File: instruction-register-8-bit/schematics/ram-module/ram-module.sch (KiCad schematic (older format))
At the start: 19 parts

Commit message: updated annotations
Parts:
- gave numbers to parts that had none: 15
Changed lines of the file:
@@
 $EndDescr
 $Comp
-L common-symbols:UM61512A U?
+L common-symbols:UM61512A U4
 U 1 1 60FE2046
 P 5375 2100
-F 0 "U?" V 5400 2125 50  0000 L CNN
+F 0 "U4" V 5400 2125 50  0000 L CNN
 F 1 "UM61512A" V 5725 800 50  0000 L CNN
 F 2 "" H 5625 0   50  0001 C CNN
@@
 $EndComp
 $Comp
-L 74xx:74LS245 U?
+L 74xx:74LS245 U5
 U 1 1 60FE803A
 P 6425 4525
-F 0 "U?" V 6700 3875 50  0000 R CNN
+F 0 "U5" V 6700 3875 50  0000 R CNN
 F 1 "74LS245" V 6525 4700 50  0000 R CNN
 F 2 "" H 6425 4525 50  0001 C CNN
@@
 	4750 1475 4750 2000
 $Comp
-L 74xx:74LS257 U?
+L 74xx:74LS257 U1
 U 1 1 61003633
 P 2050 4475
-F 0 "U?" V 2325 3650 50  0000 R CNN
+F 0 "U1" V 2325 3650 50  0000 R CNN
 F 1 "74LS257" V 2050 4625 50  0000 R CNN
 F 2 "" H 2050 4475 50  0001 C CNN
@@
 $EndComp
 $Comp
-L 74xx:74LS257 U?
+L 74xx:74LS257 U2
 U 1 1 60FF65B7
 P 4125 4475
-F 0 "U?" V 4400 3650 50  0000 R CNN
+F 0 "U2" V 4400 3650 50  0000 R CNN
 F 1 "74LS257" V 4125 4625 50  0000 R CNN
 F 2 "" H 4125 4475 50  0001 C CNN
@@
 Connection ~ 6625 5450
 $Comp
-L Switch:SW_DIP_x08 SW?
+L Switch:SW_DIP_x08 SW1
 U 1 1 6103D073
 P 1025 6625
-F 0 "SW?" H 950 6175 50  0000 L CNN
+F 0 "SW1" H 950 6175 50  0000 L CNN
 F 1 "SW_DIP_x08" H 800 7200 50  0000 L CNN
 F 2 "" H 1025 6625 50  0001 C CNN
@@
 Connection ~ 625  6925
 $Comp
-L power:GND #PWR?
+L power:GND #PWR01
 U 1 1 6105BB53
 P 625 7025
-F 0 "#PWR?" H 625 6775 50  0001 C CNN
+F 0 "#PWR01" H 625 6775 50  0001 C CNN
 F 1 "GND" H 630 6852 50  0000 C CNN
 F 2 "" H 625 7025 50  0001 C CNN
@@
 	6925 5025 7150 5025
 $Comp
-L 74xx:74LS04 U?
+L 74xx:74LS04 U3
 U 1 1 610C85D1
 P 8425 4625
-F 0 "U?" H 8425 4308 50  0000 C CNN
+F 0 "U3" H 8425 4308 50  0000 C CNN
 F 1 "74LS04" H 8425 4399 50  0000 C CNN
 F 2 "" H 8425 4625 50  0001 C CNN
@@
 $EndComp
 $Comp
-L 74xx:74LS08 U?
+L 74xx:74LS08 U7
 U 1 1 610CBDAF
 P 9100 4625
-F 0 "U?" H 9100 4308 50  0000 C CNN
+F 0 "U7" H 9100 4308 50  0000 C CNN
 F 1 "74LS08" H 9100 4399 50  0000 C CNN
 F 2 "" H 9100 4625 50  0001 C CNN
@@
 RAMe
 $Comp
-L power:GND #PWR?
+L power:GND #PWR09
 U 1 1 610E4B12
 P 7225 5075
-F 0 "#PWR?" H 7225 4825 50  0001 C CNN
+F 0 "#PWR09" H 7225 4825 50  0001 C CNN
 F 1 "GND" H 7230 4902 50  0000 C CNN
 F 2 "" H 7225 5075 50  0001 C CNN
@@
 	2650 4975 2650 5350
 $Comp
-L 74xx:74LS08 U?
+L 74xx:74LS08 U7
 U 2 1 610F99AD
 P 9100 3975
-F 0 "U?" H 9100 3658 50  0000 C CNN
+F 0 "U7" H 9100 3658 50  0000 C CNN
 F 1 "74LS08" H 9100 3749 50  0000 C CNN
 F 2 "" H 9100 3975 50  0001 C CNN
@@
 Connection ~ 9400 4300
 $Comp
-L 74xx:74LS157 U?
+L 74xx:74LS157 U6
 U 1 1 61113350
 P 7275 2475
-F 0 "U?" V 7550 1650 50  0000 R CNN
+F 0 "U6" V 7550 1650 50  0000 R CNN
 F 1 "74LS157" V 7275 2625 50  0000 R CNN
 F 2 "" H 7275 2475 50  0001 C CNN
@@
 	7875 5350 10375 5350
 $Comp
-L 74xx:74LS08 U?
+L 74xx:74LS08 U7
 U 3 1 6113AE11
 P 8500 3450
-F 0 "U?" H 8425 3775 50  0000 C CNN
+F 0 "U7" H 8425 3775 50  0000 C CNN
 F 1 "74LS08" H 8475 3675 50  0000 C CNN
 F 2 "" H 8500 3450 50  0001 C CNN
@@
 	8275 2975 8275 2475
 $Comp
-L Device:C C?
+L Device:C C1
 U 1 1 61152FA1
 P 9225 3350
-F 0 "C?" V 9375 3350 50  0000 C CNN
+F 0 "C1" V 9375 3350 50  0000 C CNN
 F 1 "0.01 µF" V 9075 3350 50  0000 C CNN
 F 2 "" H 9263 3200 50  0001 C CNN
@@
 $EndComp
 $Comp
-L Device:D_Schottky D?
+L Device:D_Schottky D1
 U 1 1 61153DF2
 P 9675 3350
-F 0 "D?" H 9675 3500 50  0000 C CNN
+F 0 "D1" H 9675 3500 50  0000 C CNN
 F 1 "BAT43" H 9675 3200 50  0000 C CNN
 F 2 "" H 9675 3350 50  0001 C CNN
@@
 	8800 3350 8900 3350
 $Comp
-L Device:R R?
+L Device:R R2
 U 1 1 6115B441
 P 8700 2975
-F 0 "R?" V 8600 2975 50  0000 C CNN
+F 0 "R2" V 8600 2975 50  0000 C CNN
 F 1 "1K" V 8700 2975 50  0000 C CNN
 F 2 "" V 8630 2975 50  0001 C CNN
@@
 Connection ~ 8275 2975
 $Comp
-L power:GND #PWR?
+L power:GND #PWR011
 U 1 1 61168423
 P 8425 2475
-F 0 "#PWR?" H 8425 2225 50  0001 C CNN
+F 0 "#PWR011" H 8425 2225 50  0001 C CNN
 F 1 "GND" H 8430 2302 50  0000 C CNN
 F 2 "" H 8425 2475 50  0001 C CNN
@@
 $EndComp
 $Comp
-L Device:R R?
+L Device:R R1
 U 1 1 611746AA
 P 8700 2475
-F 0 "R?" V 8600 2475 50  0000 C CNN
+F 0 "R1" V 8600 2475 50  0000 C CNN
 F 1 "1K" V 8700 2475 50  0000 C CNN
 F 2 "" V 8630 2475 50  0001 C CNN
@@
 $EndComp
 $Comp
-L Switch:SW_Push SW?
+L Switch:SW_Push SW2
 U 1 1 61175799
 P 9250 2475
-F 0 "SW?" H 9250 2650 50  0000 C CNN
+F 0 "SW2" H 9250 2650 50  0000 C CNN
 F 1 "SW_Push" H 9250 2400 50  0000 C CNN
 F 2 "" H 9250 2675 50  0001 C CNN
@@
 	8850 2475 9050 2475
 $Comp
-L power:VCC #PWR?
+L power:VCC #PWR012
 U 1 1 611831F1
 P 9575 2475
-F 0 "#PWR?" H 9575 2325 50  0001 C CNN
+F 0 "#PWR012" H 9575 2325 50  0001 C CNN
 F 1 "VCC" H 9590 2648 50  0000 C CNN
 F 2 "" H 9575 2475 50  0001 C CNN
@@
 Connection ~ 7275 2975
 $Comp
-L power:GND #PWR?
+L power:GND #PWR010
 U 1 1 611B2D28
 P 7375 2975
-F 0 "#PWR?" H 7375 2725 50  0001 C CNN
+F 0 "#PWR010" H 7375 2725 50  0001 C CNN
 F 1 "GND" H 7380 2802 50  0000 C CNN
 F 2 "" H 7375 2975 50  0001 C CNN
@@
 CLK
 $Comp
-L 74xx:74LS04 U?
+L 74xx:74LS04 U3
 U 2 1 611C210E
 P 6575 1550
-F 0 "U?" H 6575 1233 50  0000 C CNN
+F 0 "U3" H 6575 1233 50  0000 C CNN
 F 1 "74LS04" H 6575 1324 50  0000 C CNN
 F 2 "" H 6575 1550 50  0001 C CNN
@@
 NoConn ~ 7275 1975
 $Comp
-L common-symbols:BarGraphLED_8P BAR?
+L common-symbols:BarGraphLED_8P BAR1
 U 1 1 61200D79
 P 1150 2600
-F 0 "BAR?" V 1196 2170 50  0000 R CNN
+F 0 "BAR1" V 1196 2170 50  0000 R CNN
 F 1 "BarGraphLED_8P" V 1105 2170 50  0000 R CNN
 F 2 "" H 1150 2600 50  0001 C CNN
@@
 $EndComp
 $Comp
-L Device:R_Network08 RN?
+L Device:R_Network08 RN1
 U 1 1 6120C07B
 P 1150 2075
-F 0 "RN?" H 1538 2121 50  0000 L CNN
+F 0 "RN1" H 1538 2121 50  0000 L CNN
 F 1 "R_Network08" H 1538 2030 50  0000 L CNN
 F 2 "Resistor_THT:R_Array_SIP9" V 1625 2075 50  0001 C CNN
@@
 	3025 1875 3025 2475
 $Comp
-L power:GND #PWR?
+L power:GND #PWR03
 U 1 1 61216ED8
 P 3025 2475
-F 0 "#PWR?" H 3025 2225 50  0001 C CNN
+F 0 "#PWR03" H 3025 2225 50  0001 C CNN
 F 1 "GND" H 3030 2302 50  0000 C CNN
 F 2 "" H 3025 2475 50  0001 C CNN
@@
 	5475 2475 6175 2475
 $Comp
-L power:VCC #PWR?
+L power:VCC #PWR08
 U 1 1 612BA051
 P 6175 2475
-F 0 "#PWR?" H 6175 2325 50  0001 C CNN
+F 0 "#PWR08" H 6175 2325 50  0001 C CNN
 F 1 "VCC" H 6190 2648 50  0000 C CNN
 F 2 "" H 6175 2475 50  0001 C CNN
@@
 	6175 2475 6375 2475
 $Comp
-L power:VCC #PWR?
+L power:VCC #PWR07
 U 1 1 612BA690
 P 5625 4525
-F 0 "#PWR?" H 5625 4375 50  0001 C CNN
+F 0 "#PWR07" H 5625 4375 50  0001 C CNN
 F 1 "VCC" H 5640 4698 50  0000 C CNN
 F 2 "" H 5625 4525 50  0001 C CNN
@@
 $EndComp
 $Comp
-L power:VCC #PWR?
+L power:VCC #PWR05
 U 1 1 612BAD13
 P 3225 4475
-F 0 "#PWR?" H 3225 4325 50  0001 C CNN
+F 0 "#PWR05" H 3225 4325 50  0001 C CNN
 F 1 "VCC" H 3240 4648 50  0000 C CNN
 F 2 "" H 3225 4475 50  0001 C CNN
@@
 $EndComp
 $Comp
-L power:VCC #PWR?
+L power:VCC #PWR02
 U 1 1 612BB398
 P 1150 4475
-F 0 "#PWR?" H 1150 4325 50  0001 C CNN
+F 0 "#PWR02" H 1150 4325 50  0001 C CNN
 F 1 "VCC" H 1165 4648 50  0000 C CNN
 F 2 "" H 1150 4475 50  0001 C CNN
@@
 $EndComp
 $Comp
-L power:GND #PWR?
+L power:GND #PWR04
 U 1 1 612BC056
 P 3050 4475
-F 0 "#PWR?" H 3050 4225 50  0001 C CNN
+F 0 "#PWR04" H 3050 4225 50  0001 C CNN
 F 1 "GND" H 3055 4302 50  0000 C CNN
 F 2 "" H 3050 4475 50  0001 C CNN
@@
 $EndComp
 $Comp
-L power:GND #PWR?
+L power:GND #PWR06
 U 1 1 612BC6E3
 P 5125 4475
-F 0 "#PWR?" H 5125 4225 50  0001 C CNN
+F 0 "#PWR06" H 5125 4225 50  0001 C CNN
 F 1 "GND" H 5130 4302 50  0000 C CNN
 F 2 "" H 5125 4475 50  0001 C CNN
@@
 	10150 4300 10375 4300
 $Comp
-L 74xx:74LS04 U?
+L 74xx:74LS04 U3
 U 3 1 612D4921
 P 5150 1100
-F 0 "U?" V 5104 1280 50  0000 L CNN
+F 0 "U3" V 5104 1280 50  0000 L CNN
 F 1 "74LS04" V 5195 1280 50  0000 L CNN
 F 2 "" H 5150 1100 50  0001 C CNN

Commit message: updated based on build layout
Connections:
- net GND: now also U6.13 (I1d), U6.14 (I0d); no longer U6.2 (I0a), U6.3 (I1a)
- net MDi: now also U7.10; no longer U7.5
- net MDo: now also U7.12; no longer U7.1
- net RAMe: now also U3.9, U7.13, U7.9; no longer U3.5, U7.2, U7.4
- net at U4.24 (~OE): now also U3.8; no longer U3.6
- net at U1.15 (OE), U2.15 (OE), U4.29 (~WE): now also U3.10; no longer U3.4
- net at U5.19 (CE): now also U3.12; no longer U3.2
- net at U6.12 (Zd): no longer U3.3
- net at R1.1, SW2.1: now also U6.3 (I1a); no longer U6.13 (I1d)
- net at U6.4 (Za): now also U3.11
- net at C1.1, R2.1: now also U7.4; no longer U7.10
- new net: U3.13, U7.11
- new net: U7.5, U7.8
- new net: U6.2 (I0a), U7.6
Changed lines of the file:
@@
 $Comp
 L 74xx:74LS04 U3
-U 1 1 610C85D1
+U 6 1 610C85D1
 P 8425 4625
 F 0 "U3" H 8425 4308 50  0000 C CNN
@@
 F 2 "" H 8425 4625 50  0001 C CNN
 F 3 "http://www.ti.com/lit/gpn/sn74LS04" H 8425 4625 50  0001 C CNN
-	1    8425 4625
+	6    8425 4625
 	-1   0    0    1
 $EndComp
 $Comp
 L 74xx:74LS08 U7
-U 1 1 610CBDAF
+U 4 1 610CBDAF
 P 9100 4625
 F 0 "U7" H 9100 4308 50  0000 C CNN
@@
 F 2 "" H 9100 4625 50  0001 C CNN
 F 3 "http://www.ti.com/lit/gpn/sn74LS08" H 9100 4625 50  0001 C CNN
-	1    9100 4625
+	4    9100 4625
 	-1   0    0    1
 $EndComp
@@
 $Comp
 L 74xx:74LS08 U7
-U 2 1 610F99AD
+U 3 1 610F99AD
 P 9100 3975
 F 0 "U7" H 9100 3658 50  0000 C CNN
@@
 F 2 "" H 9100 3975 50  0001 C CNN
 F 3 "http://www.ti.com/lit/gpn/sn74LS08" H 9100 3975 50  0001 C CNN
-	2    9100 3975
+	3    9100 3975
 	-1   0    0    1
 $EndComp
@@
 $Comp
 L 74xx:74LS08 U7
-U 3 1 6113AE11
+U 2 1 6113AE11
 P 8500 3450
-F 0 "U7" H 8425 3775 50  0000 C CNN
-F 1 "74LS08" H 8475 3675 50  0000 C CNN
+F 0 "U7" H 8475 3175 50  0000 C CNN
+F 1 "74LS08" H 8475 3250 50  0000 C CNN
 F 2 "" H 8500 3450 50  0001 C CNN
 F 3 "http://www.ti.com/lit/gpn/sn74LS08" H 8500 3450 50  0001 C CNN
-	3    8500 3450
-	-1   0    0    1
+	2    8500 3450
+	-1   0    0    -1
 $EndComp
 Wire Wire Line
 	8800 3550 8800 3975
-Wire Wire Line
-	8200 3450 7575 3450
-Wire Wire Line
-	7575 3450 7575 2975
 Wire Wire Line
 	7975 2975 8275 2975
@@
 	8425 2475 8550 2475
 Wire Wire Line
-	7675 2975 7675 3125
-Wire Wire Line
-	7675 3125 9050 3125
-Wire Wire Line
-	9050 3125 9050 2475
+	9050 3225 9050 2475
 Connection ~ 9050 2475
 Wire Wire Line
-	6675 2975 6775 2975
-Wire Wire Line
-	6775 2975 6975 2975
-Connection ~ 6775 2975
-Wire Wire Line
 	6975 2975 7075 2975
-Connection ~ 6975 2975
 Wire Wire Line
 	7075 2975 7275 2975
@@
 L power:GND #PWR010
 U 1 1 611B2D28
-P 7375 2975
-F 0 "#PWR010" H 7375 2725 50  0001 C CNN
-F 1 "GND" H 7380 2802 50  0000 C CNN
-F 2 "" H 7375 2975 50  0001 C CNN
-F 3 "" H 7375 2975 50  0001 C CNN
-	1    7375 2975
-	1    0    0    -1
-$EndComp
-Connection ~ 7375 2975
+P 7675 2975
+F 0 "#PWR010" H 7675 2725 50  0001 C CNN
+F 1 "GND" H 7680 2802 50  0000 C CNN
+F 2 "" H 7675 2975 50  0001 C CNN
+F 3 "" H 7675 2975 50  0001 C CNN
+	1    7675 2975
+	1    0    0    -1
+$EndComp
 Wire Wire Line
 	9375 3350 9525 3350
@@
 $Comp
 L 74xx:74LS04 U3
-U 2 1 611C210E
-P 6575 1550
-F 0 "U3" H 6575 1233 50  0000 C CNN
-F 1 "74LS04" H 6575 1324 50  0000 C CNN
-F 2 "" H 6575 1550 50  0001 C CNN
-F 3 "http://www.ti.com/lit/gpn/sn74LS04" H 6575 1550 50  0001 C CNN
-	2    6575 1550
+U 5 1 611C210E
+P 6375 1550
+F 0 "U3" H 6375 1233 50  0000 C CNN
+F 1 "74LS04" H 6375 1324 50  0000 C CNN
+F 2 "" H 6375 1550 50  0001 C CNN
+F 3 "http://www.ti.com/lit/gpn/sn74LS04" H 6375 1550 50  0001 C CNN
+	5    6375 1550
 	-1   0    0    1
 $EndComp
 Wire Wire Line
-	7575 1975 7575 1550
-Wire Wire Line
-	7575 1550 6875 1550
-Wire Wire Line
-	6275 1550 5925 1550
+	6075 1550 5925 1550
 Wire Wire Line
 	5250 1550 5250 2000
@@
 Wire Wire Line
 	5925 1550 5250 1550
-NoConn ~ 6675 1975
+NoConn ~ 7575 1975
 NoConn ~ 6975 1975
 NoConn ~ 7275 1975
@@
 $Comp
 L 74xx:74LS04 U3
-U 3 1 612D4921
+U 4 1 612D4921
 P 5150 1100
 F 0 "U3" V 5104 1280 50  0000 L CNN
@@
 F 2 "" H 5150 1100 50  0001 C CNN
 F 3 "http://www.ti.com/lit/gpn/sn74LS04" H 5150 1100 50  0001 C CNN
-	3    5150 1100
+	4    5150 1100
 	0    1    1    0
 $EndComp
@@
 Wire Wire Line
 	5150 650  4925 650
+Wire Wire Line
+	7375 2975 7575 2975
+Connection ~ 7375 2975
+Wire Wire Line
+	7575 2975 7675 2975
+Connection ~ 7575 2975
+Connection ~ 7675 2975
+Wire Wire Line
+	6775 3225 6775 2975
+Wire Wire Line
+	6775 3225 9050 3225
+Wire Wire Line
+	6675 3450 6675 2975
+Wire Wire Line
+	6675 3450 8200 3450
+Wire Wire Line
+	6675 1975 6675 1550
 $EndSCHEMATC

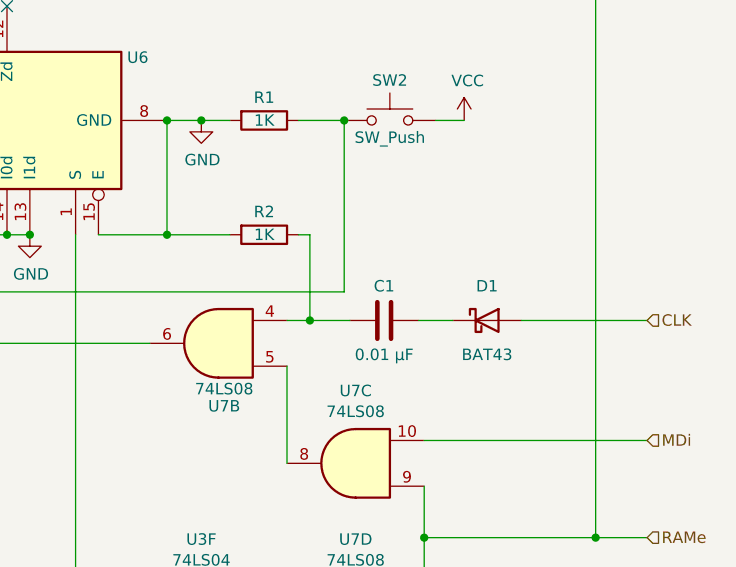
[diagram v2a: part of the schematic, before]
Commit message: removed unnecessary RC circuit on clock line
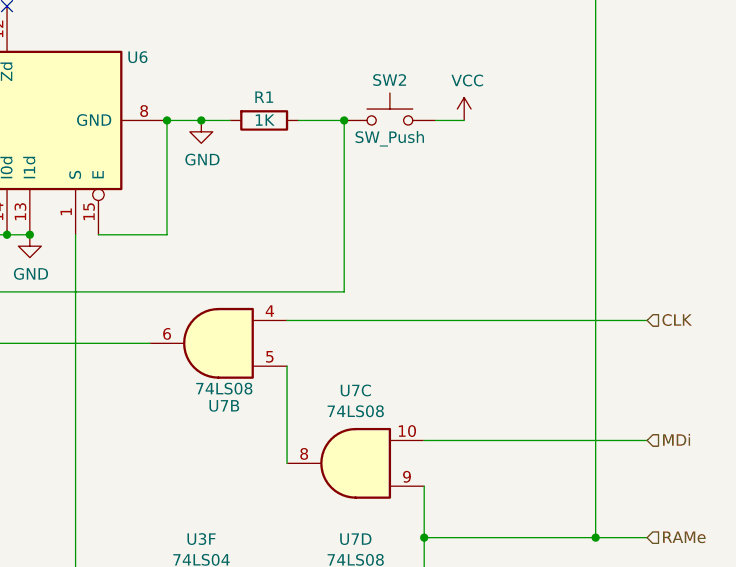
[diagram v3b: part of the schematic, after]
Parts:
- removed C1: 0.01 µF, symbol Device:C
- removed D1: BAT43, symbol Device:D_Schottky
- removed R2: 1K, symbol Device:R
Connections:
- net CLK: now also U7.4
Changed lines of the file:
@@
 	8275 2975 8275 2475
-$Comp
-L Device:C C1
-U 1 1 61152FA1
-P 9225 3350
-F 0 "C1" V 9375 3350 50  0000 C CNN
-F 1 "0.01 µF" V 9075 3350 50  0000 C CNN
-F 2 "" H 9263 3200 50  0001 C CNN
-F 3 "~" H 9225 3350 50  0001 C CNN
-	1    9225 3350
-	0    -1   -1   0
-$EndComp
-$Comp
-L Device:D_Schottky D1
-U 1 1 61153DF2
-P 9675 3350
-F 0 "D1" H 9675 3500 50  0000 C CNN
-F 1 "BAT43" H 9675 3200 50  0000 C CNN
-F 2 "" H 9675 3350 50  0001 C CNN
-F 3 "~" H 9675 3350 50  0001 C CNN
-	1    9675 3350
-	1    0    0    -1
-$EndComp
-Wire Wire Line
-	8800 3350 8900 3350
-$Comp
-L Device:R R2
-U 1 1 6115B441
-P 8700 2975
-F 0 "R2" V 8600 2975 50  0000 C CNN
-F 1 "1K" V 8700 2975 50  0000 C CNN
-F 2 "" V 8630 2975 50  0001 C CNN
-F 3 "~" H 8700 2975 50  0001 C CNN
-	1    8700 2975
-	0    1    1    0
-$EndComp
-Wire Wire Line
-	8900 3350 8900 2975
-Wire Wire Line
-	8900 2975 8850 2975
-Connection ~ 8900 3350
-Wire Wire Line
-	8900 3350 9075 3350
-Wire Wire Line
-	8550 2975 8275 2975
-Connection ~ 8275 2975
 $Comp
 L power:GND #PWR011
@@
 	1    0    0    -1
 $EndComp
-Wire Wire Line
-	9375 3350 9525 3350
-Wire Wire Line
-	9825 3350 10375 3350
 Text HLabel 10375 3350 2    50   Input ~ 0
 CLK
@@
 Wire Wire Line
 	6675 1975 6675 1550
+Wire Wire Line
+	8800 3350 10375 3350
 $EndSCHEMATC
